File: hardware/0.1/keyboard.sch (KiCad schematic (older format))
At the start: 328 parts, among them J1 USB_C_Receptacle_USB2.0, J2 SWD, Q1 BSS138, Q2 BSS138, Q3 DTC123J, SW1 SW_Push, U1 USBLC6-2SC6, U2 AP2112K-3.3, U3 STM32F303RCTx, Y1 8MHz

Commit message: layout ++
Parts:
- added BZ1: Buzzer, Buzzer_Beeper:Buzzer_Murata_PKMCS0909E4000-R1, symbol Device:Buzzer
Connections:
- net labels added: BUZZER
- wire segments 831 -> 835
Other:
- note added: "Bangers r us"
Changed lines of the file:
@@
 	1    0    0    -1
 $EndComp
+$Comp
+L Device:Buzzer BZ1
+U 1 1 5EEF1BAA
+P 16050 14500
+F 0 "BZ1" H 16202 14529 50  0000 L CNN
+F 1 "Buzzer" H 16202 14438 50  0000 L CNN
+F 2 "Buzzer_Beeper:Buzzer_Murata_PKMCS0909E4000-R1" V 16025 14600 50  0001 C CNN
+F 3 "~" V 16025 14600 50  0001 C CNN
+	1    16050 14500
+	1    0    0    -1
+$EndComp
+Text Label 18350 10550 2    50   ~ 0
+BUZZER
+Wire Wire Line
+	18350 10550 18050 10550
+Wire Wire Line
+	15950 14600 15900 14600
+Wire Wire Line
+	15900 14600 15900 14650
+$Comp
+L power:GND #PWR08
+U 1 1 5EFA84E7
+P 15900 14650
+F 0 "#PWR08" H 15900 14400 50  0001 C CNN
+F 1 "GND" H 15905 14477 50  0000 C CNN
+F 2 "" H 15900 14650 50  0001 C CNN
+F 3 "" H 15900 14650 50  0001 C CNN
+	1    15900 14650
+	1    0    0    -1
+$EndComp
+Text Label 15600 14400 0    50   ~ 0
+BUZZER
+Wire Wire Line
+	15950 14400 15600 14400
+Text Notes 15300 14200 0    100  ~ 0
+Bangers r us
 $EndSCHEMATC

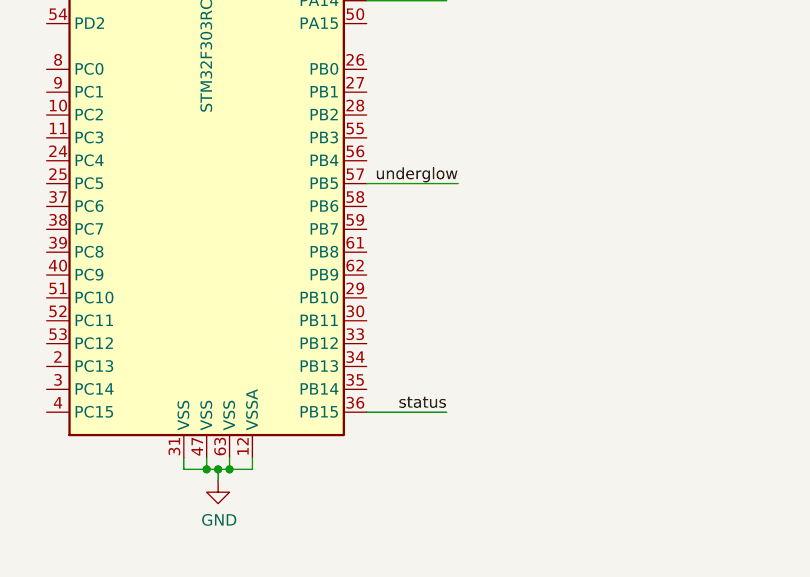
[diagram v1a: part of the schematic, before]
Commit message: unrouted = 0 with no matrix - mcu connections
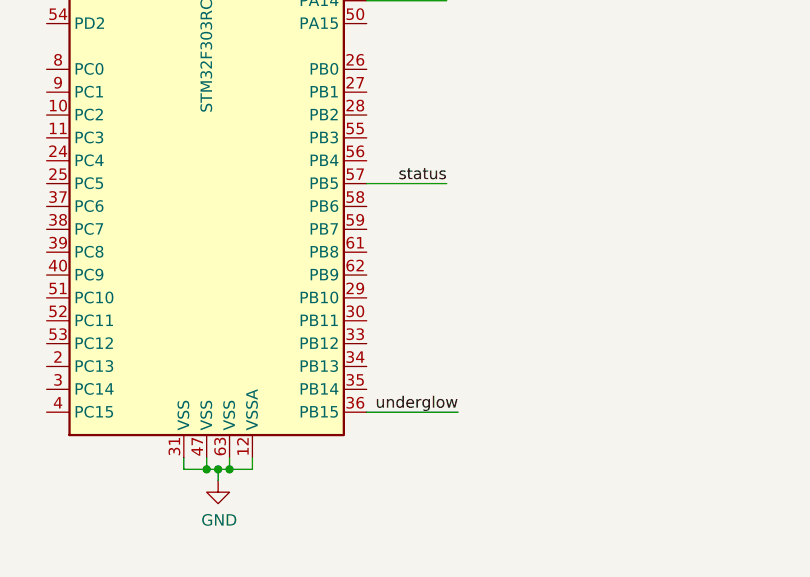
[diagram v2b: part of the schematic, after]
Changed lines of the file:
@@
 	21950 8850 22300 8850
 Wire Wire Line
-	18450 12350 18050 12350
-Text Label 18450 12350 2    50   ~ 0
+	18450 13350 18050 13350
+Text Label 18450 13350 2    50   ~ 0
 underglow
 Text Label 21950 10250 0    50   ~ 0
@@
 	21950 8200 22300 8200
 Wire Wire Line
-	18400 13350 18050 13350
-Text Label 18400 13350 2    50   ~ 0
+	18400 12350 18050 12350
+Text Label 18400 12350 2    50   ~ 0
 status
 Text Label 18400 11550 2    50   ~ 0

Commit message: layout done
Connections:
- wire segments 835 -> 843
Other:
- moved on the sheet: R9
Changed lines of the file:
@@
 XTAL_1
 Wire Wire Line
-	21950 10250 22300 10250
+	18550 10750 18050 10750
 Wire Wire Line
-	21950 10150 22300 10150
+	18550 10650 18050 10650
 Wire Wire Line
-	21950 10050 22300 10050
+	16100 13350 16650 13350
 Wire Wire Line
-	21950 9950 22300 9950
+	16100 13250 16650 13250
 Wire Wire Line
-	21950 9850 22300 9850
+	16100 13150 16650 13150
 Wire Wire Line
-	21950 9750 22300 9750
+	16100 11850 16650 11850
 Wire Wire Line
-	21950 9650 22300 9650
+	16100 11950 16650 11950
 Wire Wire Line
-	21950 9550 22300 9550
+	16100 12050 16650 12050
 Wire Wire Line
-	21950 9450 22300 9450
+	16100 12150 16650 12150
 Wire Wire Line
-	21950 9350 22300 9350
+	18550 12650 18050 12650
 Wire Wire Line
-	21950 9250 22300 9250
+	18550 12750 18050 12750
 Wire Wire Line
-	21950 9150 22300 9150
+	18550 12050 18050 12050
 Wire Wire Line
-	21950 9050 22300 9050
+	18550 12850 18050 12850
 Wire Wire Line
-	21950 8950 22300 8950
+	18550 12950 18050 12950
 Wire Wire Line
-	21950 8850 22300 8850
+	18550 13050 18050 13050
 Wire Wire Line
-	18450 13350 18050 13350
-Text Label 18450 13350 2    50   ~ 0
+	18550 13350 18050 13350
+Text Label 18550 13350 2    50   ~ 0
 underglow
-Text Label 21950 10250 0    50   ~ 0
+Text Label 18550 10750 2    50   ~ 0
 col14
-Text Label 21950 10150 0    50   ~ 0
+Text Label 18550 10650 2    50   ~ 0
 col13
-Text Label 21950 10050 0    50   ~ 0
+Text Label 16100 13350 0    50   ~ 0
 col12
-Text Label 21950 9950 0    50   ~ 0
+Text Label 16100 13250 0    50   ~ 0
 col11
-Text Label 21950 9850 0    50   ~ 0
+Text Label 16100 13150 0    50   ~ 0
 col10
-Text Label 21950 9750 0    50   ~ 0
+Text Label 16100 11850 0    50   ~ 0
 col9
-Text Label 21950 9650 0    50   ~ 0
+Text Label 16100 11950 0    50   ~ 0
 col8
-Text Label 21950 9550 0    50   ~ 0
+Text Label 16100 12050 0    50   ~ 0
 col7
-Text Label 21950 9450 0    50   ~ 0
+Text Label 16100 12150 0    50   ~ 0
 col6
-Text Label 21950 9350 0    50   ~ 0
+Text Label 18550 12650 2    50   ~ 0
 col5
-Text Label 21950 9250 0    50   ~ 0
+Text Label 18550 12750 2    50   ~ 0
 col4
-Text Label 21950 9150 0    50   ~ 0
+Text Label 18550 12050 2    50   ~ 0
 col3
-Text Label 21950 9050 0    50   ~ 0
+Text Label 18550 12850 2    50   ~ 0
 col2
-Text Label 21950 8950 0    50   ~ 0
+Text Label 18550 12950 2    50   ~ 0
 col1
-Text Label 21950 8850 0    50   ~ 0
+Text Label 18550 13050 2    50   ~ 0
 col0
-Text Label 21950 10550 0    50   ~ 0
+Text Label 18550 12150 2    50   ~ 0
 col17
-Text Label 21950 10650 0    50   ~ 0
-col18
-Wire Wire Line
-	21950 10550 22300 10550
 Wire Wire Line
-	21950 10650 22300 10650
-Text Label 21950 10350 0    50   ~ 0
+	18550 12150 18050 12150
+Text Label 18550 10850 2    50   ~ 0
 col15
-Text Label 21950 10450 0    50   ~ 0
+Text Label 16100 12250 0    50   ~ 0
 col16
 Wire Wire Line
-	21950 10350 22300 10350
+	18550 10850 18050 10850
 Wire Wire Line
-	21950 10450 22300 10450
+	16100 12250 16650 12250
 Wire Wire Line
-	21950 8700 22300 8700
+	16100 12350 16650 12350
 Wire Wire Line
-	21950 8600 22300 8600
+	18550 11850 18050 11850
 Wire Wire Line
-	21950 8500 22300 8500
+	18550 11950 18050 11950
 Wire Wire Line
-	21950 8400 22300 8400
+	16100 13050 16650 13050
 Wire Wire Line
-	21950 8300 22300 8300
+	16100 12950 16650 12950
 Wire Wire Line
-	21950 8200 22300 8200
+	16100 12850 16650 12850
 Wire Wire Line
-	18400 12350 18050 12350
-Text Label 18400 12350 2    50   ~ 0
+	18550 12350 18050 12350
+Text Label 18550 12350 2    50   ~ 0
 status
-Text Label 18400 11550 2    50   ~ 0
+Text Label 18550 11550 2    50   ~ 0
 SWDCLK
-Text Label 18400 11450 2    50   ~ 0
+Text Label 18550 11450 2    50   ~ 0
 SWDIO
 Wire Wire Line
-	18050 11550 18400 11550
+	18050 11550 18550 11550
 Wire Wire Line
-	18050 11450 18400 11450
-Text Label 18400 11350 2    50   ~ 0
+	18050 11450 18550 11450
+Text Label 18550 11350 2    50   ~ 0
 USB_D+
-Text Label 18400 11250 2    50   ~ 0
+Text Label 18550 11250 2    50   ~ 0
 USB_D-
 Wire Wire Line
-	18050 11250 18400 11250
-Text Label 21950 8700 0    50   ~ 0
+	18050 11250 18550 11250
+Text Label 16100 12350 0    50   ~ 0
 row5
-Text Label 21950 8600 0    50   ~ 0
+Text Label 18550 11850 2    50   ~ 0
 row4
-Text Label 21950 8500 0    50   ~ 0
+Text Label 18550 11950 2    50   ~ 0
 row3
-Text Label 21950 8400 0    50   ~ 0
+Text Label 16100 13050 0    50   ~ 0
 row2
-Text Label 21950 8300 0    50   ~ 0
+Text Label 16100 12950 0    50   ~ 0
 row1
-Text Label 21950 8200 0    50   ~ 0
+Text Label 16100 12850 0    50   ~ 0
 row0
 Connection ~ 19750 4300
@@
 $EndComp
 Wire Wire Line
-	21950 10750 22300 10750
-Text Label 21950 10750 0    50   ~ 0
+	18550 12450 18050 12450
+Text Label 18550 12450 2    50   ~ 0
 col19
 Wire Wire Line
@@
 Text Label 10900 15750 0    50   ~ 0
 MCU_RST
-Text Label 21950 10900 0    50   ~ 0
+Text Label 18550 11650 2    50   ~ 0
 MCU_RST
 Wire Wire Line
-	21950 10900 22300 10900
+	18550 11650 18050 11650
 $Comp
 L Device:R R7
@@
 Programming
 Wire Wire Line
-	18050 11350 18600 11350
+	18050 11350 18750 11350
 $Comp
 L Device:R R9
 U 1 1 6AAD8F7E
-P 18600 11150
-F 0 "R9" H 18670 11196 50  0000 L CNN
-F 1 "1K5" H 18670 11105 50  0000 L CNN
-F 2 "Resistor_SMD:R_0603_1608Metric" V 18530 11150 50  0001 C CNN
-F 3 "~" H 18600 11150 50  0001 C CNN
-	1    18600 11150
+P 18750 11150
+F 0 "R9" H 18820 11196 50  0000 L CNN
+F 1 "1K5" H 18820 11105 50  0000 L CNN
+F 2 "Resistor_SMD:R_0603_1608Metric" V 18680 11150 50  0001 C CNN
+F 3 "~" H 18750 11150 50  0001 C CNN
+	1    18750 11150
 	1    0    0    -1
 $EndComp
 Wire Wire Line
-	18600 11300 18600 11350
+	18750 11300 18750 11350
 Wire Wire Line
-	18600 11000 18600 10950
+	18750 11000 18750 10950
 $Comp
 L power:+3V3 #PWR03
 U 1 1 6ABD0C3B
-P 18600 10950
-F 0 "#PWR03" H 18600 10800 50  0001 C CNN
-F 1 "+3V3" H 18615 11123 50  0000 C CNN
-F 2 "" H 18600 10950 50  0001 C CNN
-F 3 "" H 18600 10950 50  0001 C CNN
-	1    18600 10950
+P 18750 10950
+F 0 "#PWR03" H 18750 10800 50  0001 C CNN
+F 1 "+3V3" H 18765 11123 50  0000 C CNN
+F 2 "" H 18750 10950 50  0001 C CNN
+F 3 "" H 18750 10950 50  0001 C CNN
+	1    18750 10950
 	1    0    0    -1
 $EndComp
@@
 	1    0    0    -1
 $EndComp
-Text Label 18350 10550 2    50   ~ 0
+Text Label 18550 10550 2    50   ~ 0
 BUZZER
 Wire Wire Line
-	18350 10550 18050 10550
+	18550 10550 18050 10550
 Wire Wire Line
 	15950 14600 15900 14600
@@
 Text Notes 15300 14200 0    100  ~ 0
 Bangers r us
+Text Label 18550 11150 2    50   ~ 0
+ENC3_A_DB
+Text Label 18550 11050 2    50   ~ 0
+ENC3_B_DB
+Text Label 16100 12750 0    50   ~ 0
+ENC2_A_DB
+Text Label 18550 10950 2    50   ~ 0
+ENC2_B_DB
+Text Label 16100 12550 0    50   ~ 0
+ENC1_A_DB
+Text Label 16100 12650 0    50   ~ 0
+ENC1_B_DB
+Text Label 18550 13150 2    50   ~ 0
+ENC0_A_DB
+Text Label 18550 13250 2    50   ~ 0
+ENC0_B_DB
+Wire Wire Line
+	18550 13150 18050 13150
+Wire Wire Line
+	18550 13250 18050 13250
+Wire Wire Line
+	16100 12550 16650 12550
+Wire Wire Line
+	16100 12750 16650 12750
+Wire Wire Line
+	18550 10950 18050 10950
+Wire Wire Line
+	18550 11150 18050 11150
+Wire Wire Line
+	18550 11050 18050 11050
+Wire Wire Line
+	16100 12650 16650 12650
+Wire Wire Line
+	18550 12250 18050 12250
+Text Label 18550 12250 2    50   ~ 0
+col18
 $EndSCHEMATC

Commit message: graphics added
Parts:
- added D14: LED, LED_SMD:LED_0603_1608Metric, symbol Device:LED
- added LOGO4: BSILK, graphics:back_silk_v0, symbol Mechanical:MountingHole
- added R11: 1K5, Resistor_SMD:R_0603_1608Metric, symbol Device:R
- C1, C2: JLCSMT (none) -> C15849
- C10, C11, C12, C13, C14, C15, C16, C17, C6, C7, C8, C9: JLCSMT (none) -> C14663; LCSC (none) -> C14663; MPN (none) -> CC0603KRX7R9BB104; Manufacturer (none) -> YAGEO
- C18, C19, C20, C21, C22, C23, C24, C25, C27, C28, C29, C30, C32, C33, C34, C35, C36, C37, C38, C39: JLCSMT (none) -> C14663; LCSC C15849 -> C14663; MPN CL10A105MP8NNNC -> CC0603KRX7R9BB104; Manufacturer Samsung Electro-Mechanics -> YAGEO
- C26: renamed from 10u1; JLCSMT (none) -> C19666; LCSC (none) -> C19666; MPN (none) -> CL10A475KO8NNNC; Manufacturer (none) -> Samsung Electro-Mechanics
- C3, C40: JLCSMT (none) -> C19702; LCSC (none) -> C19702; MPN (none) -> CL10A106KP8NNNC; Manufacturer (none) -> Samsung Electro-Mechanics
- C4, C5: JLCSMT (none) -> C1653; LCSC (none) -> C1653; MPN (none) -> CL10C220JB8NNNC; Manufacturer (none) -> Samsung Electro-Mechanics
- D1, D10, D11, D12, D13, D15, D17, D2, D20, D3, D4, D5, D6, D7, D8, D9: JLCSMT (none) -> C114586
- D24: JLCSMT (none) -> C81598; LCSC (none) -> C81598; MPN (none) -> 1N4148W; Manufacturer (none) -> Semtech
- D_0, D_1, D_10, D_100, D_101, D_102, D_103, D_104, D_105, D_106, D_107, D_108, D_11, D_110, D_112, D_114, D_12, D_13, D_14, D_15, D_16, D_17, D_18, D_19, D_2, D_20, D_21, D_22, D_23, D_24, D_25, D_26, D_27, D_28, D_29, D_3, D_30, D_31, D_32, D_33, D_34, D_35, D_36, D_37, D_38, D_39, D_4, D_40, D_41, D_42, D_43, D_44, D_45, D_46, D_47, D_48, D_49, D_5, D_50, D_51, D_52, D_53, D_54, D_55, D_56, D_57, D_58, D_6, D_60, D_61, D_62, D_63, D_64, D_65, D_66, D_67, D_68, D_69, D_7, D_70, D_71, D_72, D_73, D_74, D_75, D_76, D_77, D_78, D_79, D_8, D_80, D_81, D_82, D_83, D_84, D_85, D_86, D_87, D_88, D_89, D_9, D_90, D_91, D_92, D_93, D_94, D_95, D_97, D_98, D_99: value D -> 1N4148; JLCSMT (none) -> C81598; LCSC (none) -> C81598; MPN (none) -> 1N4148W; Manufacturer (none) -> Semtech
- H1, H10, H11, H12, H2, H3, H4, H5, H6, H7, H8, H9, J2, K_0, K_1, K_10, K_100, K_101, K_102, K_103, K_104, K_105, K_106, K_107, K_108, K_109, K_11, K_110, K_111, K_112, K_113, K_114, K_115, K_12, K_13, K_14, K_15, K_16, K_17, K_18, K_19, K_2, K_20, K_21, K_22, K_23, K_24, K_25, K_26, K_27, K_28, K_29, K_3, K_30, K_31, K_32, K_33, K_34, K_35, K_36, K_37, K_38, K_39, K_4, K_40, K_41, K_42, K_43, K_44, K_45, K_46, K_47, K_48, K_49, K_5, K_50, K_51, K_52, K_53, K_54, K_55, K_56, K_57, K_58, K_59, K_6, K_60, K_61, K_62, K_63, K_64, K_65, K_66, K_67, K_68, K_69, K_7, K_70, K_71, K_72, K_73, K_74, K_75, K_76, K_77, K_78, K_79, K_8, K_80, K_81, K_82, K_83, K_84, K_85, K_86, K_87, K_88, K_89, K_9, K_90, K_91, K_92, K_93, K_94, K_95, K_96, K_97, K_98, K_99: DNP (none) -> DNP
- R1, R2, R3, R4: DigiKey CR0603-JW-103ELFCT-ND -> (none); JLCSMT (none) -> C25804; LCSC C144116 -> C25804; MPN CR0603-JW-103ELF -> 0603WAF1002T5E; Manufacturer Bourns -> Uniroyal Elec
- R10, R7, R9: JLCSMT (none) -> C22843; LCSC (none) -> C22843; MPN (none) -> 0603WAF1501T5E; Manufacturer (none) -> Uniroyal Elec
- R5, R6: JLCSMT (none) -> C23186; LCSC (none) -> C23186; MPN (none) -> 0603WAF5101T5E; Manufacturer (none) -> Uniroyal Elec
- R8: JLCSMT (none) -> C25803; LCSC (none) -> C25803; MPN (none) -> 0603WAF1003T5E; Manufacturer (none) -> Uniroyal Elec
- RN1, RN2, RN3, RN4: JLCSMT (none) -> C29718; LCSC (none) -> C29718; MPN (none) -> 4D03WGJ0103T5E; Manufacturer (none) -> Uniroyal Elec
- U3: JLCSMT (none) -> C65361; LCSC (none) -> C65361; MPN (none) -> STM32F303RCT6; Manufacturer (none) -> STMicroelectronics
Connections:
- net +3V3: now also R11.1
- net GND: now also D14.1 (K)
- new net: D14.2 (A), R11.2
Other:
- moved on the sheet: BZ1

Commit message: merged LEDs into one string
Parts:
- removed Q2: BSS138, Package_TO_SOT_SMD:SOT-23, symbol Transistor_FET:BSS138
- removed R3, R4: 10K, Resistor_SMD:R_0603_1608Metric, symbol Device:R
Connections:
- net status is gone; now on net col19: U3.57 (PB5)
- net VBUS: now also C40.2, F1.2, J1.A4 (VBUS), J1.A9 (VBUS), J1.B4 (VBUS), J1.B9 (VBUS), U1.5 (VBUS)
- net col19: no longer U3.58 (PB6)
- net at D12.2 (DOUT): now also D21.4 (DIN)
- no-connect marks 4 -> 12
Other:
- moved on the sheet: C18, C19, C20, C21, C22, C23, C24, C25, C27, C28, C29, C30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
